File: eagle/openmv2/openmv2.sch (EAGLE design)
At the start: 82 parts, among them J3 CON_HEADER_1X03, J4 CON_HEADER_1X03, Q1 MOSFET, U1 TPS2114APW, U10 IS42S16800E, U2 USD-47571, U3 BEAD, U4 TPS768, U5 BEAD, U6 BEAD, U7 STM32F429, U8 VREG_25, U9 OV2640, X1 USB-MICROB

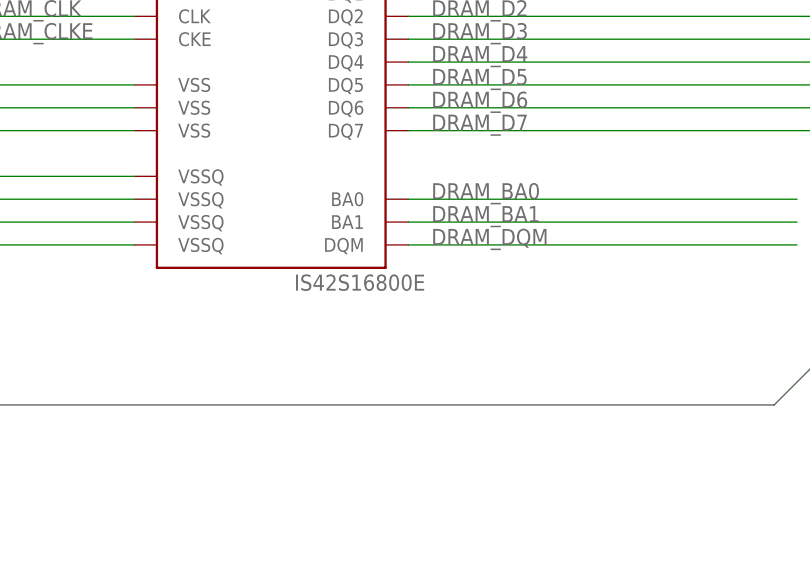
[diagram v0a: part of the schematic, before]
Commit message: Fix SDRAM part-no
* Issue #29
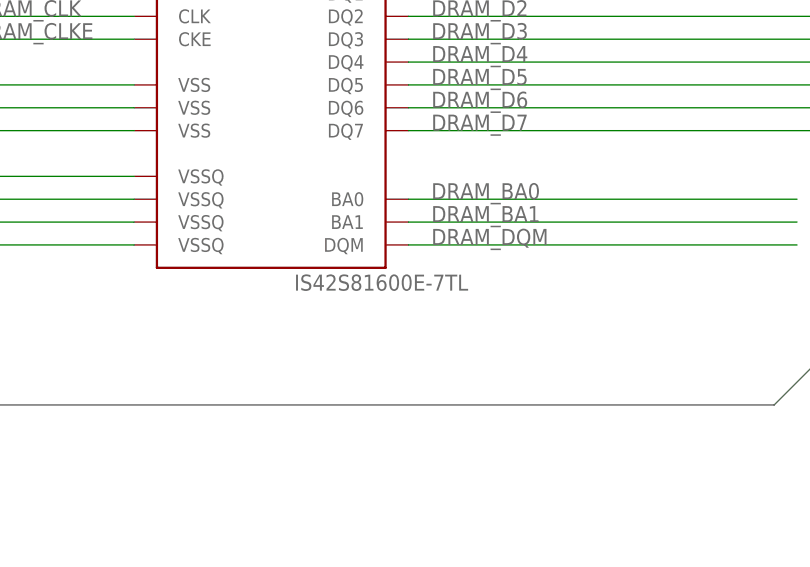
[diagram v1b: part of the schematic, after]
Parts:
- U10: value IS42S16800E -> IS42S81600E-7TL
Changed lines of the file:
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@@
 <part name="C14" library="sfe" deviceset="CAP" device="0402-CAP" value="0.1uF"/>
 <part name="GND3" library="sfe" deviceset="GND" device=""/>
-<part name="U10" library="mux" deviceset="IS42S16800E" device=""/>
+<part name="U10" library="mux" deviceset="IS42S16800E" device="" value="IS42S81600E-7TL"/>
 <part name="U9" library="omnivision" deviceset="OV2640" device=""/>
 <part name="C16" library="sfe" deviceset="CAP" device="0402-CAP" value="0.1uF"/>

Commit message: Rename Eagle files
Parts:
- removed C12, C21: 100uF, sfe:CAP_POL1206
- removed C25, C26, C27, C28, C29, C31, C32, C35, C36, C37, C43: 0.1uF, sfe:CAP0402-CAP
- removed C30: 10uF, sfe:CAP0805
- removed C33, C34: 2.2uF, sfe:CAP0402-CAP
- removed C38: 100uF, sfe:CAP_POL3528
- removed H1, H8: MOUNT-PAD-ROUND2.8, holes:MOUNT-PAD-ROUND2.8
- removed R12: 1K, sfe:RESISTOR0402-RES
- removed R4: 10ohm, iofault:RESISTOR0402-RES
- removed RN2, RN8: (no value), resistor-dil:4R-NCAT16
- removed U$1: LENSMOUNT, omnivision:LENSMOUNT
- removed U$14, U$15, U$16, U$17, U$19, U$20: FIDUCIAL, adafruit:FIDUCIAL
- removed U10: IS42S81600E-7TL, mux:IS42S16800E
- removed U5: BEAD, heka:BEAD
- removed X1: USB-MICROB, sfe:USB-MICROB
- added C48, C49: 2.2uF, sfe:CAP0603-CAP
- added D1: BAT54C, diode:BAT54C
- added JP3, JP4: (no value), pinhead:PINHD-1X8
- added JP5, JP6, JP7, JP8: FIDUCIAL1X2, sfe:FIDUCIAL1X2
- added R2: 10k, sfe:RESISTOR0603-RES
- added U12: STM32F427-LQFP100, mux:STM32F407LQFP100
- added X2: USB-MICROB, sfe:USB-MICROB
- C1: value 0.1uF -> 22uF; device sfe:CAP0402-CAP -> sfe:CAP0805
- C10, C13, C14, C15, C16, C17, C18, C19, C20, C4, C5, C6, C7, C8, C9: device sfe:CAP0402-CAP -> sfe:CAP0603-CAP
- C11: value 100uF -> 22uF; device sfe:CAP_POL3528 -> sfe:CAP0805
- C2: value 0.1uF -> 4.7uF; device sfe:CAP0402-CAP -> sfe:CAP0603-CAP
- C23, C24: value 10uF -> 4.7uF; device sfe:CAP0402-CAP -> sfe:CAP0603-CAP
- C3: device sfe:CAP_POL1206 -> sfe:CAP1206
- C40, C41: value 18pF -> 12pF; device sfe:CAP0402-CAP -> sfe:CAP0603-CAP
- JP1, JP2: value (none) -> FIDUCIAL1X2; device pinhead:PINHD-1X10 -> sfe:FIDUCIAL1X2
- LOGO1: value OSHW_LOGO_FILLX0200-NT -> OSHW_LOGO_FILLX0150-NT; device iofault:OSHW_LOGO_FILLX0200-NT -> iofault:OSHW_LOGO_FILLX0150-NT
- R1: value 10K -> 10ohm; device sfe:RESISTOR0402-RES -> sfe:RESISTOR0603-RES
- R5: device sfe:RESISTOR0402-RES -> sfe:RESISTOR0603-RES
- RN4: value (none) -> 220R; device resistor-dil:4R-NCAT16 -> resistor-dil:4R-NEXBV8V
- RN5, RN6: value (none) -> 10K; device resistor-dil:4R-NCAT16 -> resistor-dil:4R-NEXBV8V
- RN7: value (none) -> 10K
- U1: value TPS2114APW -> LENSMOUNT20MM; device mux:TPS2115APW -> omnivision:LENSMOUNT20MM
- U3, U6: value BEAD -> (none); device heka:BEAD -> sfe:INDUCTOR0603
- U4: value TPS768 -> BD33IA; device mux:TPS768 -> mux:BD33IA
- U7: value STM32F429 -> (none); device stm32:STM32F429 -> sfe:INDUCTOR0603
- U8: value VREG_25 -> VREG_28
- Y1: device mux:CRYSTAL -> mux:CRYSTAL2.5X2.0
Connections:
- removed net ADC12_IN14: JP1.8, U7G$2.PC4/ETH_RMII_RX_D0/ETH_MII_RX_D0/ADC12_IN14
- removed net ADC12_IN15: JP1.7, U7G$2.PC5/ETH_RMII_RX_D1/ETH_MII_RX_D1/ADC12_IN15
- removed net ADC12_IN5: U7G$2.PA5/SPI1_SCK/OTG_HS_ULPI_CK/TIM2_CH1/TIM2_ETR/TIM8_CHIN/ADC12_IN5
- removed net DCMI_SCL: RN7B.1, U7G$2.PB10/SPI2_SCK/I2S2_CK/I2C2_SCL/USART3_TX/OTG_HS_ULPI_D3/TIM2_CH3, U9.SCL
- removed net DCMI_SDA: RN7A.1, U7G$2.PB11/I2C2_SDA/USART3_RX/OTG_HS_ULPI_D4/ETH_RMII_TX_EN/TIM2_CH4, U9.SDA
- removed net DRAM_A0: U10.A0, U7G$3.PF0/I2C2_SDA/FMC_A0
- removed net DRAM_A1: U10.A1, U7G$3.PF1/I2C2_SCL/FMC_A1
- removed net DRAM_A10: U10.A10, U7G$3.PG0/FMC_A10
- removed net DRAM_A11: U10.A11, U7G$3.PG1/FMC_A11
- removed net DRAM_A2: U10.A2, U7G$3.PF2/I2C2_SMBA/FSMC_A2
- removed net DRAM_A3: U10.A3, U7G$3.PF3/FMC_A3
- removed net DRAM_A4: U10.A4, U7G$3.PF4/FMC_A4
- removed net DRAM_A5: U10.A5, U7G$3.PF5/FMC_A5
- removed net DRAM_A6: U10.A6, U7G$3.PF12/FMC_A6
- removed net DRAM_A7: U10.A7, U7G$3.PF13/FMC_A7
- removed net DRAM_A8: U10.A8, U7G$3.PF14/FMC_A8
- removed net DRAM_A9: U10.A9, U7G$3.PF15/FMC_A9
- removed net DRAM_BA0: U10.BA0, U7G$3.PG4/FMC_A14/FMC_BA0
- removed net DRAM_BA1: U10.BA1, U7G$3.PG5/FMC_A15/FMC_BA1
- removed net DRAM_CAS: U10.!CAS, U7G$3.PG15/USART6_CTS/DCMI_D13/FMC_SDNCAS
- removed net DRAM_CLK: U10.CLK, U7G$3.PG8/SPI6_NSS/USART6_RTS/ETH_PPS_OUT/FMC_SDCLK
- removed net DRAM_CLKE: U10.CKE, U7G$3.PC3/SPI2_MOSI/I2S2_SD/OTG_HS_ULPI_NXT/ETH_MII_TX_CLK/FMC_SDCKE0
- removed net DRAM_CS: R1.2, U10.!CS, U7G$3.PC2/SPI2_MISO/I2S2EXT_SD/OTG_HS_ULPI_DIR/ETH_MII_TXD2/FMC_SDNE0
- removed net DRAM_D0: U10.DQ0, U7G$3.PD14/FMC_D0/TIM4_CH3
- removed net DRAM_D1: U10.DQ1, U7G$3.PD15/FMC_D1/TIM4_CH4
- removed net DRAM_D2: U10.DQ2, U7G$3.PD0/FMC_D2/CAN1_RX
- removed net DRAM_D3: U10.DQ3, U7G$3.PD1/FMC_D3/CAN1_TX
- removed net DRAM_D4: U10.DQ4, U7G$3.PE7/FMC_D4/TIM1_ETR/UART7_RX
- removed net DRAM_D5: U10.DQ5, U7G$3.PE8/FSMC_D5/TIM1_CH1N/UART7_TX
- removed net DRAM_D6: U10.DQ6, U7G$3.PE9/FMC_D6/TIM1_CH1
- removed net DRAM_D7: U10.DQ7, U7G$3.PE10/FMC_D7/TIM1_CH2N
- removed net DRAM_DQM: U10.DQM, U7G$3.PE0/TIM4_ETR/UART8_RX/FMC_NBL0/DCMI_D2
- removed net DRAM_RAS: U10.!RAS, U7G$3.PF11/DCMI_12/SPI5_MOSI/FMC_SDNRAS
- removed net DRAM_WE: U10.!WE, U7G$3.PC0/OTG_HS_ULPI_STP/ADC123_IN10/FMC_SDNWE
- removed net FS_DN: U7G$2.PA11/TIM1_CH4/USART1_CTS/CAN1_RX/LCD_R4/OTG_FS_DM, X1.D-
- removed net N$15: U7G$2.PG13/SPI6_SCK/USART6_CTS/ETH_MII_TXD0/ETH_RMII_TXD0/FMC_A24
- removed net N$17: U7G$2.PG7/FSMC_INT3/DCMI_D13
- removed net N$18: U7G$2.PF6/TIM10_CH1/SPI5_NSS/SAI1_SD_B/UART7_RX/FMC_NIORD
- removed net N$19: U7G$2.PG6/FSMC_INT2/DCMI_D12
- removed net N$20: JP1.1, RN8A.1
- removed net N$21: JP1.2, RN8B.1
- removed net N$22: U5.1, X1.VBUS
- removed net N$23: JP1.3, RN8C.1
- removed net N$24: JP1.4, RN8D.1
- removed net N$25: U7G$2.PD6/SPI3_MOSI/I2S3_SD/USART2_RX/FMC_NWAIT/DCMI_D10
- removed net N$26: R12.2, U1.LIMIT
- removed net N$27: U7G$2.PF7/TIM11_CH1/SPI5_SCK/SAI1_MCLK_B/UART7_TX/FMC_NREG
- removed net N$28: U7G$2.PF8/TIM13_CH1/SPI5_MISO/SAI1_SCK_B/FMC_NIOWR
- removed net SPI4_MISO: RN8C.2, U7G$2.PE5/TRACED2/FSMC_A21/TIM9_CH1/DCMI_D6/SPI4_MISO
- removed net SPI4_MOSI: RN8D.2, U7G$2.PE6/TRACED3/FSMC_A22/TIM9_CH2/DCMI_D7/SPI4_MOSI
- removed net SPI4_NSS: RN8B.2, U7G$2.PE3/TRACED0/FSMC_A19
- removed net SPI4_SCK: RN8A.2, U7G$2.PE2/TRACECLK/FSMC_A23/ETH_MII_TXD3/SPI4_SCK
- removed net TIM12_CH1: U7G$2.PB14/SPI2_MISO/TIM1_CH2N/TIM12_CH1/OTG_HS_DM/USART3_RTS/TIM8_CH2N
- removed net TIM12_CH2: U7G$2.PB15/SPI2_MOSI/I2S2_SD/TIM1_CH3N/TIM8_CH3N/TIM12_CH2/OTG_HS_DP
- removed net USART2_RX: JP1.6, U7G$2.PA3/USART2_RX/TIM5_CH4/TIM9_CH2/TIM2_CH4/OTG_HS_ULPI_D0
- removed net USART2_TX: JP1.5, U7G$2.PA2/USART2_TX/TIM5_CH3/TIM9_CH1/TIM2_CH3/ETH_MDIO
- removed net USART3_RX: JP2.7, U7G$2.PD9/FMC_D14/USART3_RX
- removed net USART3_TX: JP2.8, U7G$2.PD8/FMC_D13/USART3_TX
- removed net VBAT: J3.2, J4.2, JP2.9, U1.IN2
- new net DAC: JP4.7, U12.PA5/SPI1_SCK/OTG_HS_ULPI_CK/TIM2_CH1_ETR/TIM8_CHIN/ADC12_IN5
- new net EXPST: U12.PD8/FSMC_D13/USART3_TX, U9.EXPST_B
- new net FREX: U12.PD9/FSMC_D14/USART3_RX, U9.FREX
- new net FS_DM: U12.PA11/USART1_CTS/CAN1_RX/TIM1_CH4/OTG_FS_DM, X2.D-
- new net I2C1_SCL: RN7B.1, U12.PB8/TIM4_CH3/SDIO_D4/TIM10_CH1/DCMI_D6/OTG_FS_SCL/ETH_MII_TXD3, U9.SCL
- new net I2C1_SDA: RN7A.1, U12.PB9/SPI2_NSS/I2S2_WS/TIM4_CH4/TIM11_CH1/SDIO_D5/DCMI_D7/I2C1_SDA, U9.SDA
- new net I2C2_SCL: JP4.5, U12.PB10/SPI2_SCK/I2S2_CK/I2C2_SCL/USART3_TX/OTG_HS_ULPI_D3/TIM2_CH3
- new net I2C2_SDA: JP4.6, U12.PB11/I2C2_SDA/USART3_RX/OTG_HS_ULPI_D4/ETH_RMII_TX_EN/TIM2_CH4
- new net RAW: D1.A1, J3.2, J4.2, JP3.7
- new net SPI2_MISO: JP4.2, U12.PB14/SPI2_MISO/TIM1_CH2N/TIM12_CH1/OTG_HS_DMUSART3_/53/RTS/TIM8_CH2N
- new net SPI2_MOSI: JP4.1, U12.PB15/SPI2_MOSI/I2S2_SD/TIM1_CH3N/TIM8_CH3N/TIM12_CH2/OTG_HS_DP
- new net SPI2_NSS: JP4.4, U12.PB12/SPI2_NSS/I2S2_WS/I2C2_SMBA/USART3_CK/TIM1_BKIN/CAN2_RX
- new net SPI2_SCLK: JP4.3, U12.PB13/SPI2_SCK/I2S2_CK/USART3_CTS/TIM1_CH1N/CAN2_TX/OTG_HS_ULPI_D6
- new net STROBE: U12.PD3/FSMC_CLK/USART2_CTS, U9.STROBE
- net BOOT0: now also JP3.3, RN5A.2, U12.BOOT0; no longer JP2.3, RN2C.2, U7G$1.BOOT0
- net DCMI_CLK: now also U12.PA8/MCO1/USART1_CK/TIM1_CH1/I2C3_SCL/OTG_FS_SOF; no longer U7G$2.PA8/MCO1/USART1_CK/TIM1_CH1/I2C3_SCL/OTG_FS_SOF
- net DCMI_D0: now also U12.PC6/I2S2_MCK/TIM8_CH1/SDIO_D6/USART6_TX/DCMI_D0/TIM3_CH1; no longer U7G$4.PC6/I2S2_MCK/TIM8_CH1/SDIO_D6/USART6_TX/DCMI_D0
- net DCMI_D1: now also U12.PC7/I2S3_MCK/TIM8_CH2/SDIO_D7/USART6_RX/DCMI_D1/TIM3_CH2; no longer U7G$4.PC7/I2S3_MCK/TIM8_CH2/SDIO_D7/USART6_RX/DCMI_D1
- net DCMI_D2: now also U12.PE0/TIM4_ETR/FSMC_NBL0/DCMI_D2; no longer U7G$4.PG10/LCD_G3/FMC_NCE4_1/FMC_NE3/DCMI_D2/LCD_B2
- net DCMI_D3: now also U12.PE1/FSMC_NBL1/DCMI_D3; no longer U7G$4.PG11/ETH_MII_TX_EN/ETH_RMII_TX_ENFMC_NCE4_2/DCMI_D3
- net DCMI_D4: now also U12.PE4/TRACED1/FSMC_A20/DCMI_D4; no longer U7G$4.PE4/TRACED1/FSMC_A20/DCMI_D4/SPI4_NSS
- net DCMI_D5: now also U12.PB6/I2C1_SCL/TIM4_CH1/CAN2_TX/OTG_FS_INTN/DCMI_D5/USART1_TX; no longer U7G$4.PD3/SPI2_SCK/I2S2_CK/USART2_CTS/FMC_CLK/DCMI_D5
- net DCMI_D6: now also U12.PE5/TRACED2/FSMC_A21/TIM9_CH1/DCMI_D6; no longer U7G$4.PB8/TIM4_CH3/TIM10_CH1/I2C1_SCL/CAN1_RX/SDIO_D4/DCMI_D6
- net DCMI_D7: now also U12.PE6/TRACED3/FSMC_A22/TIM9_CH2/DCMI_D7; no longer U7G$4.PB9/TIM11_CH1/I2C1_SDA/SPI2_NSS/I2S2_WS/SDIO_D5/DCMI_D7
- net DCMI_HSYNC: now also U12.PA4/SPI1_NSS/SPI3_NSS/USART2_CK/DCMI_HSYNC/OTG_HS_SOF/I2S3_WS; no longer U7G$4.PA4/SPI1_NSS/SPI3_NSS/USART2_CK/DCMI_HSYNC
- net DCMI_PCLK: now also U12.PA6/SPI1_MISO/TIM8_BKIN/TIM13_CH1/DCMI_PIXCLK/TIM3_CH1/TIM1_BKIN; no longer U7G$4.PA6/SPI1_MISO/TIM8_BKIN/TIM13_CH1/DCMI_PIXCLK
- net DCMI_PWDN: now also U12.PB5/I2C1_SMBA/TIM3_CH2/SPI1_MOSI/SPI3_MOSI/DCMI_D10/I2S3_SD; no longer U7G$2.PA10/TIM1_CH3/USART1_RX/OTG_FS_ID/DCMI_D1
- net DCMI_RST: now also U12.PA10/USART1_RX/TIM1_CH3/OTG_FS_ID/DCMI_D1; no longer U7G$2.PA15/JTDI/SPI3_NSS/I2S3_WS/TIM2_CH1_ETR/SPI1_NSS
- net DCMI_VSYNC: now also U12.PB7/I2C1_SDA/FSMC_NL/DCMI_VSYNC/USART1_RX/TIM4_CH2; no longer U7G$4.PB7/TIM4_CH2//I2C1_SDA/USART1_RX//FMC_NL/DCMI_VSYNC
- net FS_DP: now also U12.PA12/USART1_RTS/CAN1_TX/TIM1_ETR/OTG_FS_DP, X2.D+; no longer U7G$2.PA12/TIM1_ETR/USART1_RTS/CAN1_TX/LCD_R5/OTG_FS_DP, X1.D+
- net GND: now also C11.1, C3.2, C48.2, C49.2, JP3.8, R2.1, RN5A.1, U12.PB2/BOOT1, U12.VSS@1, U12.VSS@2, U12.VSS@3, U12.VSS@4, U12.VSSA, U4.GND@1, U4.GND@2, X2.GND; no longer C11.-, C12.-, C21.-, C25.2, C26.2, C27.2, C28.1, C29.2, C3.-, C30.2, C31.2, C32.2, C33.2, C34.2, C35.2, C36.2, C37.2, C38.-, C43.2, H1.MOUNT, H2.MOUNT, H6.MOUNT, H8.MOUNT, JP1.10, JP2.10, R12.1, RN2A.1, RN2C.1, U$1.P$1, U$1.P$2, U1.D1, U1.GND, U10.VSS@1, U10.VSS@2, U10.VSS@3, U10.VSSQ@1, U10.VSSQ@2, U10.VSSQ@3, U10.VSSQ@4, U4.EN, U4.GND, U7G$1.BOOT1, U7G$1.VSS@1, U7G$1.VSS@2, U7G$1.VSS@3, U7G$1.VSS@4, U7G$1.VSS@5, U7G$1.VSS@6, U7G$1.VSS@7, U7G$1.VSS@8, U7G$1.VSS@9, U7G$1.VSSA, U9.EXPST_B, U9.FREX, X1.GND
- net LED_B: now also U12.PC1/ETH_MDC/ADC123_IN11; no longer U7G$2.PB5/TIM3_CH2/SPI1_MOSI/SPI3_MOSI/I2S3_SD/DCMI_D10/FMC_SDCKE1
- net LED_G: now also U12.PC2/SPI2_MISO/OTG_HS_ULPI_DIR/TH_MII_TXD2/I2S2EXT_SD/ADC123_IN12; no longer U7G$2.PB6/TIM4_CH1/I2C1_SCL/USART1_TX/CAN2_TX/FMC_SDNE1/DCMI_D5
- net LED_IR: now also U12.PE2/TRACECLK/FSMC_A23/ETH_MII_TXD3; no longer U7G$2.PB3/JTDO/TRACESWO/SPI3_SCK/I2S3_CK/TIM2_CH2/SPI1_SCK
- net LED_R: now also U12.PC0/OTG_HS_ULPI_STP/ADC123_IN10; no longer U7G$2.PB4/NJTRST/TIM3_CH1/SPI1_MISO/SPI3_MISO/I2S3EXT_SD
- net N$10: now also R1.2; no longer R4.1
- net N$12: now also C4.1, C5.1, U12.VDDA, U12.VREF, U3.1; no longer U7G$2.PG12/SPI6_MISO/USART6_RTS/LCD_B4/FMC_NE4/LCD_B1
- net N$14: now also R1.1; no longer R4.2
- net N$2: now also U12.PH1/OSC_OUT; no longer U7G$1.PH0/OSC_IN
- net N$4: now also U12.PH0/OSC_IN; no longer U7G$1.PH1/OSC_OUT
- net N$5: now also R2.2
- net N$7: now also U7.1, X2.VBUS; no longer C4.1, C5.1, U3.1, U7G$1.VDDA, U7G$1.VREF+
- net NRST: now also JP3.4, RN5B.2, U12.NRST; no longer JP2.4, RN2D.2, U7G$1.NRST
- net SDIO_CLK: now also U12.PC12/UART5_TX/SDIO_CK/DCMI_D9/SPI3_MOSI/I2S3_SD/USART3_CK; no longer U7G$2.PC12/UART5_TX/SDIO_CK/DCMI_D9/SPI3_MOSI/I2S3_SD/USART3_CK
- net SDIO_CMD: now also U12.PD2/TIM3_ETR/UART5_RXSDIO_CMD/DCMI_D11; no longer U7G$2.PD2/TIM3_ETR/UART5_RX/SDIO_CMD/DCMI_D11
- net SDIO_D0: now also RN5C.2, U12.PC8/TIM8_CH3/SDIO_D0/TIM3_CH3/USART6_CK/DCMI_D2; no longer RN5B.2, U7G$2.PC8/TIM8_CH3/SDIO_D0/TIM3_CH3/USART6_CK/DCMI_D2
- net SDIO_D1: now also U12.PC9/I2S_CKIN/MCO2/TIM8_CH4/SDIO_D1/I2C3_SDA/DCMI_D3/TIM3_CH4; no longer U7G$2.PC9/I2S_CKIN/MCO2/TIM8_CH4/SDIO_D1/I2C3_SDA/DCMI_D3/TIM3_CH4
- net SDIO_D2: now also U12.PC10/SPI3_SCK/I2S3_CK/UART4_TX/SDIO_D2/DCMI_D8/USART3_TX; no longer U7G$2.PC10/SPI3_SCK/I2S3_CK/UART4_TX/SDIO_D2/DCMI_D8/USART3_TX
- net SDIO_D3: now also U12.PC11/UART4_RX/SPI3_MISO/SDIO_D3/DCMI_D4/USART3_RX/I2S3EXT_SD; no longer U7G$2.PC11/UART4_RX/SPI3_MISO/SDIO_D3/DCMI_D4
- net SD_CD: now also U12.PA15/JTDI/SPI3_NSS/I2S3_WS/TIM2_CH1_ETR/SPI1_NSS; no longer U7G$2.PG9/USART6_RX/FMC_NE2/FMC_NCE3/DCMI_VSYNC
- net SWCLK: now also JP3.1, U12.PA14/JTCK-SWCLK; no longer JP2.1, RN2A.2, U7G$1.PA14/JTCK-SWCLK
- net SWDIO: now also JP3.2, U12.PA13/JTMS-SWDIO; no longer JP2.2, RN2B.2, U7G$1.PA13/JTMS-SWDIO
- net TIM4_CH1: now also JP3.6, U12.PD12/FSMC_A17/TIM4_CH1/USART3_RTS; no longer JP2.6, U7G$2.PD12/FMC_A17/TIM4_CH1/USART3_RTS
- net TIM4_CH2: now also JP3.5, U12.PD13/FSMC_A18/TIM4_CH2; no longer JP2.5, U7G$2.PD13/FMC_A18/TIM4_CH2
- net VBUS: now also D1.A2, U12.PA9/USART1_TX/TIM1_CH2/I2C3_SMBA/DCMI_D0/OTG_FS_VBUS, U7.2; no longer C43.1, U1.IN1, U5.2, U7G$2.PA9/TIM1_CH2/I2C3_SMBA/USART1_TX/DCMI_D0/OTG_FS_VBUS
- net VCAP1: now also C49.1, U12.VCAP@1; no longer C34.1, U7G$1.VCAP@1
- net VCAP2: now also C48.1, U12.VCAP@2; no longer C33.1, U7G$1.VCAP@2
- net VCC: now also C11.2, C3.1, JP4.8, U12.VBAT, U12.VDD@1, U12.VDD@2, U12.VDD@3, U12.VDD@4, U12.VDD@5, U12.VDD@6, U4.VO, U4.VOS; no longer C12.+, C2.1, C21.+, C25.1, C26.1, C27.1, C28.2, C29.1, C3.+, C30.1, C31.1, C32.1, C35.1, C36.1, C37.1, C38.+, JP1.9, R1.1, RN2B.1, RN2D.1, RN5A.1, U10.VDD@1, U10.VDD@2, U10.VDD@3, U10.VDDQ@1, U10.VDDQ@2, U10.VDDQ@3, U10.VDDQ@4, U4.OUT@1, U4.OUT@2, U7G$1.PDR_ON, U7G$1.VBAT, U7G$1.VDD@1, U7G$1.VDD@10, U7G$1.VDD@11, U7G$1.VDD@12, U7G$1.VDD@2, U7G$1.VDD@3, U7G$1.VDD@4, U7G$1.VDD@5, U7G$1.VDD@6, U7G$1.VDD@7, U7G$1.VDD@8, U7G$1.VDD@9
- net VIN: now also C2.1, D1.CC, U4.EN, U4.VCC; no longer C11.+, U1.OUT, U4.IN@1, U4.IN@2
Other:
- note removed: "USB lines are terminated in driver"
- moved on the sheet: C1, C10, C13, C14, C15, C16, C17, C18, C19, C2, C20, C23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

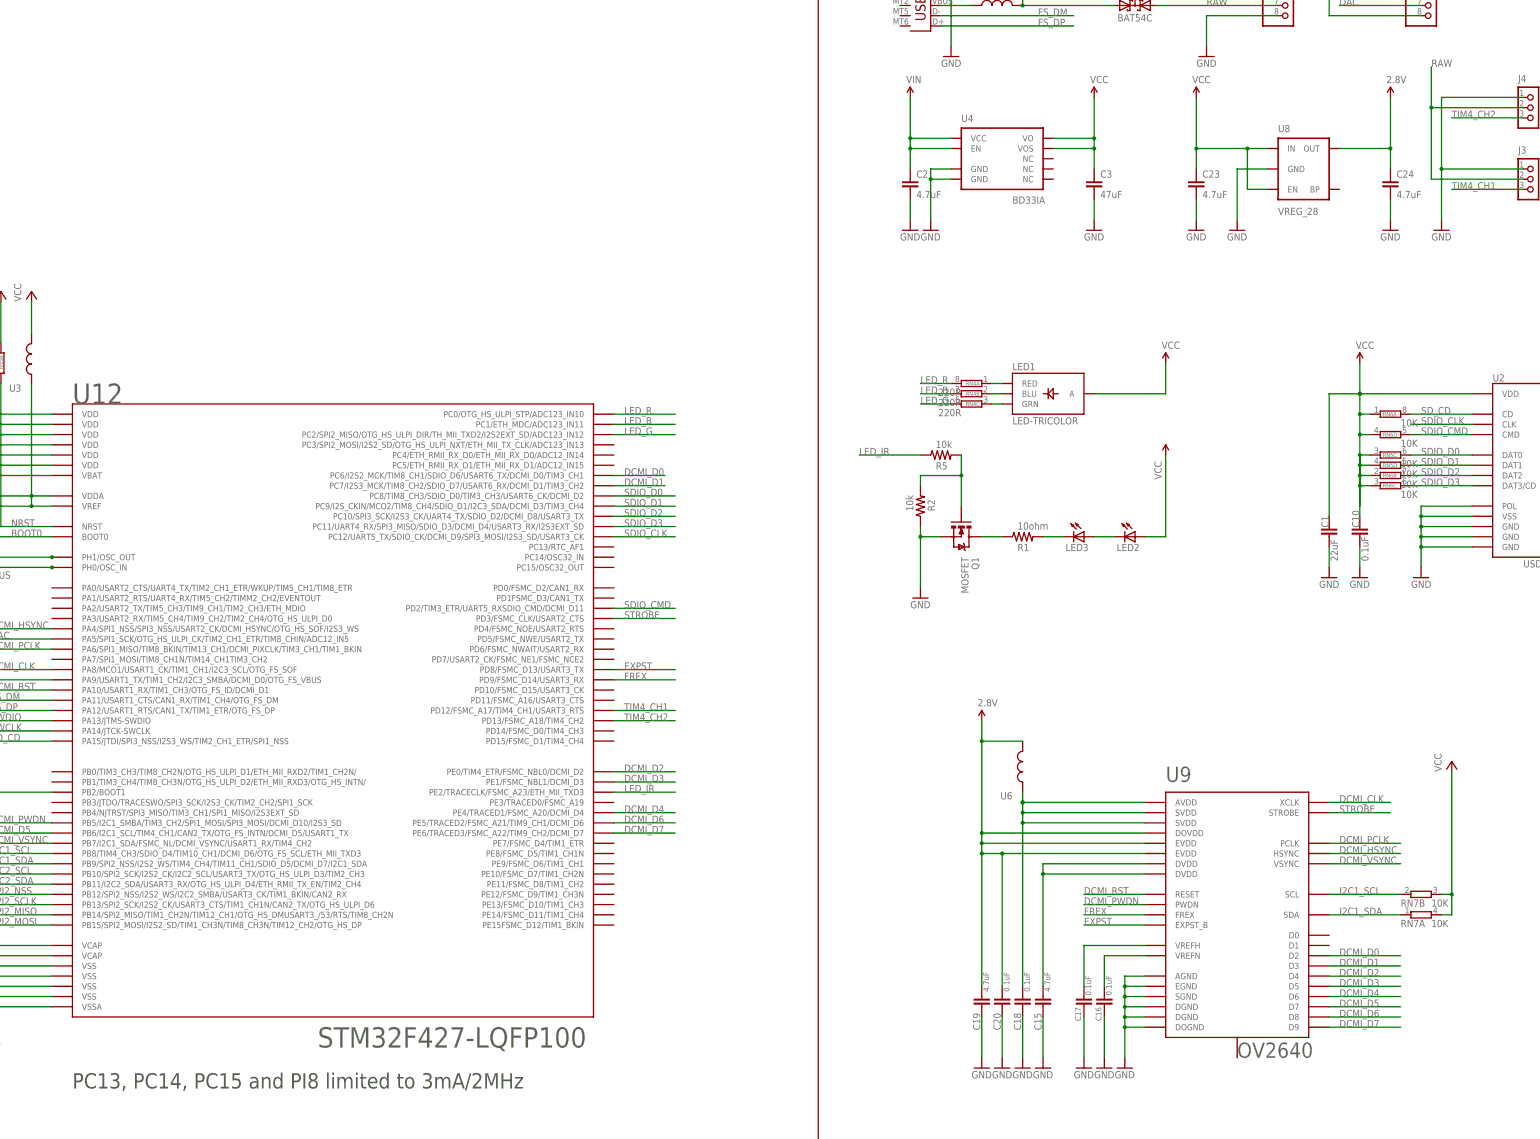
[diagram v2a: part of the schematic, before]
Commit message: Update Eagle files.
* Add OpenMV2-R5
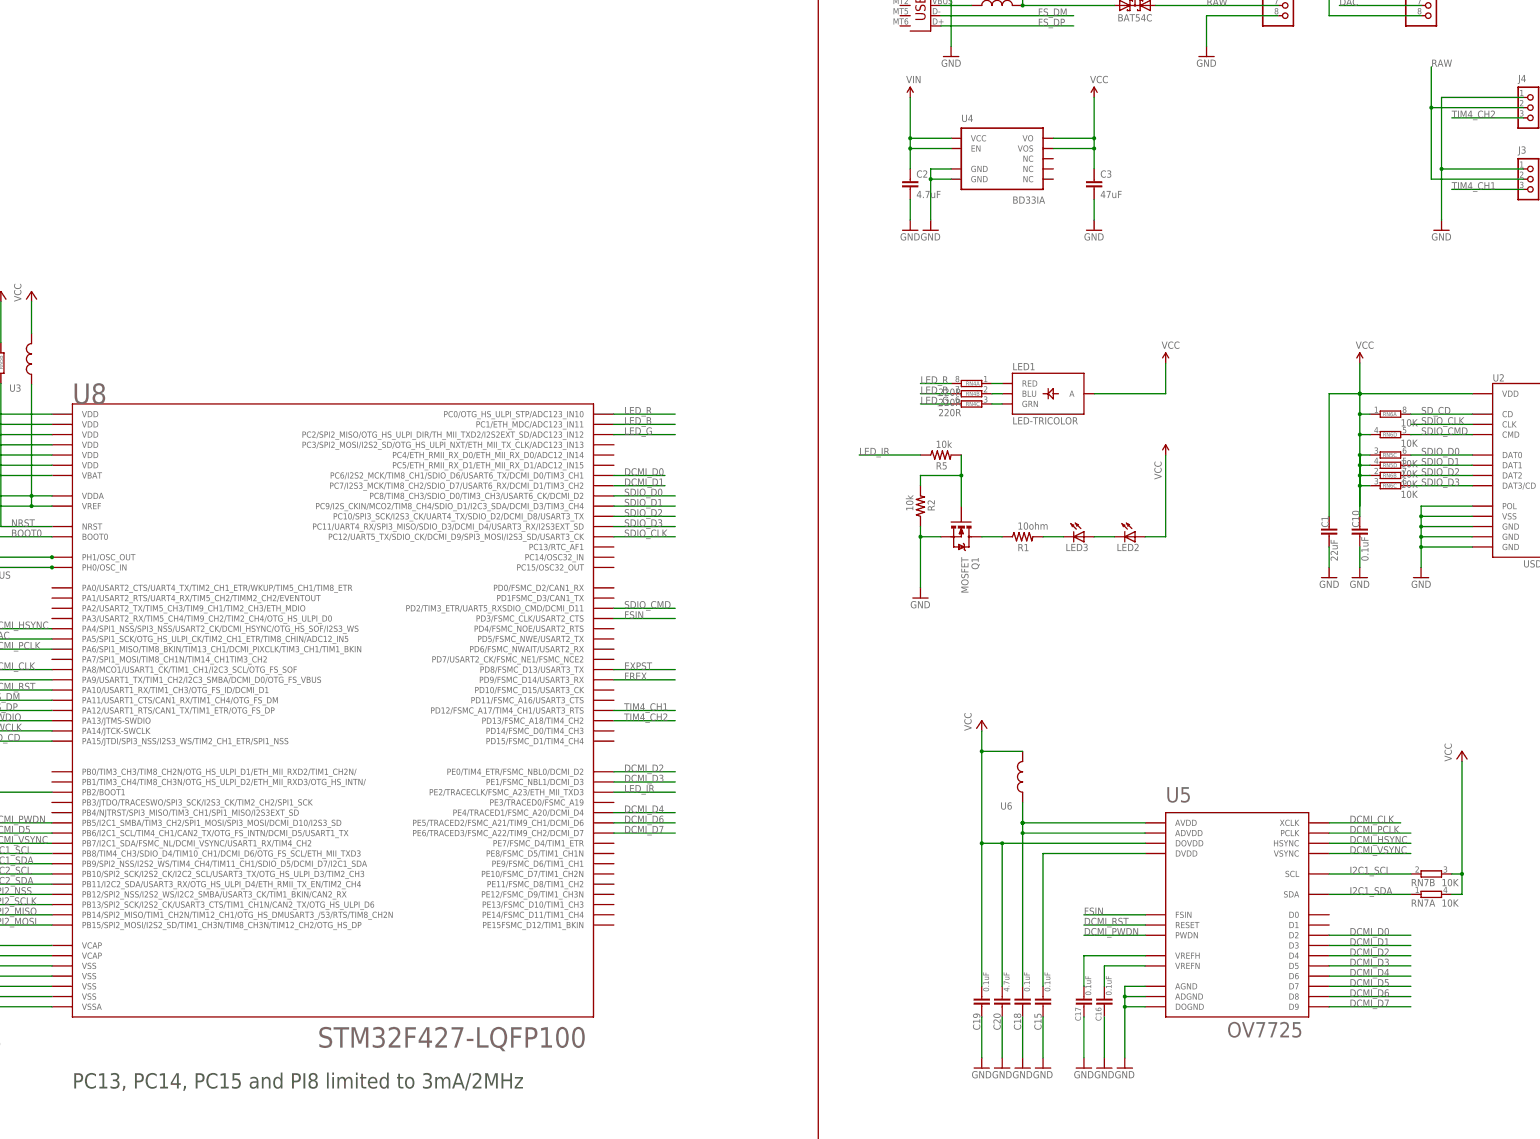
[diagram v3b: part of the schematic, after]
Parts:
- removed C23, C24: 4.7uF, sfe:CAP0603-CAP
- removed U12: STM32F427-LQFP100, mux:STM32F407LQFP100
- removed U9: OV2640, omnivision:OV2640
- added U5: OV7725, omnivision:OV7725
- C15, C19: value 4.7uF -> 0.1uF
- C20: value 0.1uF -> 4.7uF
- U8: value VREG_28 -> STM32F427-LQFP100; device sfe:V_REG_LDOSMD -> mux:STM32F407LQFP100
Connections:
- removed net 2.8V: C19.1, C20.1, C24.1, U6.2, U8.OUT, U9.DOVDD, U9.EVDD@1, U9.EVDD@2
- removed net N$6: C15.1, U9.DVDD@1, U9.DVDD@2
- removed net STROBE: U12.PD3/FSMC_CLK/USART2_CTS, U9.STROBE
- new net FSIN: U5.FSIN, U8.PD3/FSMC_CLK/USART2_CTS
- new net N$15: C15.1, U5.DVDD
- net BOOT0: now also U8.BOOT0; no longer U12.BOOT0
- net DAC: now also U8.PA5/SPI1_SCK/OTG_HS_ULPI_CK/TIM2_CH1_ETR/TIM8_CHIN/ADC12_IN5; no longer U12.PA5/SPI1_SCK/OTG_HS_ULPI_CK/TIM2_CH1_ETR/TIM8_CHIN/ADC12_IN5
- net DCMI_CLK: now also U5.XCLK, U8.PA8/MCO1/USART1_CK/TIM1_CH1/I2C3_SCL/OTG_FS_SOF; no longer U12.PA8/MCO1/USART1_CK/TIM1_CH1/I2C3_SCL/OTG_FS_SOF, U9.XCLK
- net DCMI_D0: now also U5.D2, U8.PC6/I2S2_MCK/TIM8_CH1/SDIO_D6/USART6_TX/DCMI_D0/TIM3_CH1; no longer U12.PC6/I2S2_MCK/TIM8_CH1/SDIO_D6/USART6_TX/DCMI_D0/TIM3_CH1, U9.D2
- net DCMI_D1: now also U5.D3, U8.PC7/I2S3_MCK/TIM8_CH2/SDIO_D7/USART6_RX/DCMI_D1/TIM3_CH2; no longer U12.PC7/I2S3_MCK/TIM8_CH2/SDIO_D7/USART6_RX/DCMI_D1/TIM3_CH2, U9.D3
- net DCMI_D2: now also U5.D4, U8.PE0/TIM4_ETR/FSMC_NBL0/DCMI_D2; no longer U12.PE0/TIM4_ETR/FSMC_NBL0/DCMI_D2, U9.D4
- net DCMI_D3: now also U5.D5, U8.PE1/FSMC_NBL1/DCMI_D3; no longer U12.PE1/FSMC_NBL1/DCMI_D3, U9.D5
- net DCMI_D4: now also U5.D6, U8.PE4/TRACED1/FSMC_A20/DCMI_D4; no longer U12.PE4/TRACED1/FSMC_A20/DCMI_D4, U9.D6
- net DCMI_D5: now also U5.D7, U8.PB6/I2C1_SCL/TIM4_CH1/CAN2_TX/OTG_FS_INTN/DCMI_D5/USART1_TX; no longer U12.PB6/I2C1_SCL/TIM4_CH1/CAN2_TX/OTG_FS_INTN/DCMI_D5/USART1_TX, U9.D7
- net DCMI_D6: now also U5.D8, U8.PE5/TRACED2/FSMC_A21/TIM9_CH1/DCMI_D6; no longer U12.PE5/TRACED2/FSMC_A21/TIM9_CH1/DCMI_D6, U9.D8
- net DCMI_D7: now also U5.D9, U8.PE6/TRACED3/FSMC_A22/TIM9_CH2/DCMI_D7; no longer U12.PE6/TRACED3/FSMC_A22/TIM9_CH2/DCMI_D7, U9.D9
- net DCMI_HSYNC: now also U5.HSYNC, U8.PA4/SPI1_NSS/SPI3_NSS/USART2_CK/DCMI_HSYNC/OTG_HS_SOF/I2S3_WS; no longer U12.PA4/SPI1_NSS/SPI3_NSS/USART2_CK/DCMI_HSYNC/OTG_HS_SOF/I2S3_WS, U9.HSYNC
- net DCMI_PCLK: now also U5.PCLK, U8.PA6/SPI1_MISO/TIM8_BKIN/TIM13_CH1/DCMI_PIXCLK/TIM3_CH1/TIM1_BKIN; no longer U12.PA6/SPI1_MISO/TIM8_BKIN/TIM13_CH1/DCMI_PIXCLK/TIM3_CH1/TIM1_BKIN, U9.PCLK
- net DCMI_PWDN: now also U5.PWDN, U8.PB5/I2C1_SMBA/TIM3_CH2/SPI1_MOSI/SPI3_MOSI/DCMI_D10/I2S3_SD; no longer U12.PB5/I2C1_SMBA/TIM3_CH2/SPI1_MOSI/SPI3_MOSI/DCMI_D10/I2S3_SD, U9.PWDN
- net DCMI_RST: now also U5.RESET, U8.PA10/USART1_RX/TIM1_CH3/OTG_FS_ID/DCMI_D1; no longer U12.PA10/USART1_RX/TIM1_CH3/OTG_FS_ID/DCMI_D1, U9.RESET
- net DCMI_VSYNC: now also U5.VSYNC, U8.PB7/I2C1_SDA/FSMC_NL/DCMI_VSYNC/USART1_RX/TIM4_CH2; no longer U12.PB7/I2C1_SDA/FSMC_NL/DCMI_VSYNC/USART1_RX/TIM4_CH2, U9.VSYNC
- net EXPST: now also U8.PD8/FSMC_D13/USART3_TX; no longer U12.PD8/FSMC_D13/USART3_TX, U9.EXPST_B
- net FREX: now also U8.PD9/FSMC_D14/USART3_RX; no longer U12.PD9/FSMC_D14/USART3_RX, U9.FREX
- net FS_DM: now also U8.PA11/USART1_CTS/CAN1_RX/TIM1_CH4/OTG_FS_DM; no longer U12.PA11/USART1_CTS/CAN1_RX/TIM1_CH4/OTG_FS_DM
- net FS_DP: now also U8.PA12/USART1_RTS/CAN1_TX/TIM1_ETR/OTG_FS_DP; no longer U12.PA12/USART1_RTS/CAN1_TX/TIM1_ETR/OTG_FS_DP
- net GND: now also U5.ADGND, U5.AGND, U5.DOGND, U8.PB2/BOOT1, U8.VSS@1, U8.VSS@2, U8.VSS@3, U8.VSS@4, U8.VSSA; no longer C23.2, C24.2, U12.PB2/BOOT1, U12.VSS@1, U12.VSS@2, U12.VSS@3, U12.VSS@4, U12.VSSA, U8.GND, U9.AGND, U9.DGND@1, U9.DGND@2, U9.DOGND, U9.EGND, U9.SGND
- net I2C1_SCL: now also U5.SCL, U8.PB8/TIM4_CH3/SDIO_D4/TIM10_CH1/DCMI_D6/OTG_FS_SCL/ETH_MII_TXD3; no longer U12.PB8/TIM4_CH3/SDIO_D4/TIM10_CH1/DCMI_D6/OTG_FS_SCL/ETH_MII_TXD3, U9.SCL
- net I2C1_SDA: now also U5.SDA, U8.PB9/SPI2_NSS/I2S2_WS/TIM4_CH4/TIM11_CH1/SDIO_D5/DCMI_D7/I2C1_SDA; no longer U12.PB9/SPI2_NSS/I2S2_WS/TIM4_CH4/TIM11_CH1/SDIO_D5/DCMI_D7/I2C1_SDA, U9.SDA
- net I2C2_SCL: now also U8.PB10/SPI2_SCK/I2S2_CK/I2C2_SCL/USART3_TX/OTG_HS_ULPI_D3/TIM2_CH3; no longer U12.PB10/SPI2_SCK/I2S2_CK/I2C2_SCL/USART3_TX/OTG_HS_ULPI_D3/TIM2_CH3
- net I2C2_SDA: now also U8.PB11/I2C2_SDA/USART3_RX/OTG_HS_ULPI_D4/ETH_RMII_TX_EN/TIM2_CH4; no longer U12.PB11/I2C2_SDA/USART3_RX/OTG_HS_ULPI_D4/ETH_RMII_TX_EN/TIM2_CH4
- net LED_B: now also U8.PC1/ETH_MDC/ADC123_IN11; no longer U12.PC1/ETH_MDC/ADC123_IN11
- net LED_G: now also U8.PC2/SPI2_MISO/OTG_HS_ULPI_DIR/TH_MII_TXD2/I2S2EXT_SD/ADC123_IN12; no longer U12.PC2/SPI2_MISO/OTG_HS_ULPI_DIR/TH_MII_TXD2/I2S2EXT_SD/ADC123_IN12
- net LED_IR: now also U8.PE2/TRACECLK/FSMC_A23/ETH_MII_TXD3; no longer U12.PE2/TRACECLK/FSMC_A23/ETH_MII_TXD3
- net LED_R: now also U8.PC0/OTG_HS_ULPI_STP/ADC123_IN10; no longer U12.PC0/OTG_HS_ULPI_STP/ADC123_IN10
- net N$1: now also U5.VREFH; no longer U9.VREFH
- net N$12: now also U8.VDDA, U8.VREF; no longer U12.VDDA, U12.VREF
- net N$13: now also U5.ADVDD, U5.AVDD; no longer U9.AVDD, U9.SVDD@1, U9.SVDD@2
- net N$2: now also U8.PH1/OSC_OUT; no longer U12.PH1/OSC_OUT
- net N$3: now also U5.VREFN; no longer U9.VREFN
- net N$4: now also U8.PH0/OSC_IN; no longer U12.PH0/OSC_IN
- net NRST: now also U8.NRST; no longer U12.NRST
- net SDIO_CLK: now also U8.PC12/UART5_TX/SDIO_CK/DCMI_D9/SPI3_MOSI/I2S3_SD/USART3_CK; no longer U12.PC12/UART5_TX/SDIO_CK/DCMI_D9/SPI3_MOSI/I2S3_SD/USART3_CK
- net SDIO_CMD: now also U8.PD2/TIM3_ETR/UART5_RXSDIO_CMD/DCMI_D11; no longer U12.PD2/TIM3_ETR/UART5_RXSDIO_CMD/DCMI_D11
- net SDIO_D0: now also U8.PC8/TIM8_CH3/SDIO_D0/TIM3_CH3/USART6_CK/DCMI_D2; no longer U12.PC8/TIM8_CH3/SDIO_D0/TIM3_CH3/USART6_CK/DCMI_D2
- net SDIO_D1: now also U8.PC9/I2S_CKIN/MCO2/TIM8_CH4/SDIO_D1/I2C3_SDA/DCMI_D3/TIM3_CH4; no longer U12.PC9/I2S_CKIN/MCO2/TIM8_CH4/SDIO_D1/I2C3_SDA/DCMI_D3/TIM3_CH4
- net SDIO_D2: now also U8.PC10/SPI3_SCK/I2S3_CK/UART4_TX/SDIO_D2/DCMI_D8/USART3_TX; no longer U12.PC10/SPI3_SCK/I2S3_CK/UART4_TX/SDIO_D2/DCMI_D8/USART3_TX
- net SDIO_D3: now also U8.PC11/UART4_RX/SPI3_MISO/SDIO_D3/DCMI_D4/USART3_RX/I2S3EXT_SD; no longer U12.PC11/UART4_RX/SPI3_MISO/SDIO_D3/DCMI_D4/USART3_RX/I2S3EXT_SD
- net SD_CD: now also U8.PA15/JTDI/SPI3_NSS/I2S3_WS/TIM2_CH1_ETR/SPI1_NSS; no longer U12.PA15/JTDI/SPI3_NSS/I2S3_WS/TIM2_CH1_ETR/SPI1_NSS
- net SPI2_MISO: now also U8.PB14/SPI2_MISO/TIM1_CH2N/TIM12_CH1/OTG_HS_DMUSART3_/53/RTS/TIM8_CH2N; no longer U12.PB14/SPI2_MISO/TIM1_CH2N/TIM12_CH1/OTG_HS_DMUSART3_/53/RTS/TIM8_CH2N
- net SPI2_MOSI: now also U8.PB15/SPI2_MOSI/I2S2_SD/TIM1_CH3N/TIM8_CH3N/TIM12_CH2/OTG_HS_DP; no longer U12.PB15/SPI2_MOSI/I2S2_SD/TIM1_CH3N/TIM8_CH3N/TIM12_CH2/OTG_HS_DP
- net SPI2_NSS: now also U8.PB12/SPI2_NSS/I2S2_WS/I2C2_SMBA/USART3_CK/TIM1_BKIN/CAN2_RX; no longer U12.PB12/SPI2_NSS/I2S2_WS/I2C2_SMBA/USART3_CK/TIM1_BKIN/CAN2_RX
- net SPI2_SCLK: now also U8.PB13/SPI2_SCK/I2S2_CK/USART3_CTS/TIM1_CH1N/CAN2_TX/OTG_HS_ULPI_D6; no longer U12.PB13/SPI2_SCK/I2S2_CK/USART3_CTS/TIM1_CH1N/CAN2_TX/OTG_HS_ULPI_D6
- net SWCLK: now also U8.PA14/JTCK-SWCLK; no longer U12.PA14/JTCK-SWCLK
- net SWDIO: now also U8.PA13/JTMS-SWDIO; no longer U12.PA13/JTMS-SWDIO
- net TIM4_CH1: now also U8.PD12/FSMC_A17/TIM4_CH1/USART3_RTS; no longer U12.PD12/FSMC_A17/TIM4_CH1/USART3_RTS
- net TIM4_CH2: now also U8.PD13/FSMC_A18/TIM4_CH2; no longer U12.PD13/FSMC_A18/TIM4_CH2
- net VBUS: now also U8.PA9/USART1_TX/TIM1_CH2/I2C3_SMBA/DCMI_D0/OTG_FS_VBUS; no longer U12.PA9/USART1_TX/TIM1_CH2/I2C3_SMBA/DCMI_D0/OTG_FS_VBUS
- net VCAP1: now also U8.VCAP@1; no longer U12.VCAP@1
- net VCAP2: now also U8.VCAP@2; no longer U12.VCAP@2
- net VCC: now also C19.1, C20.1, U5.DOVDD, U6.2, U8.VBAT, U8.VDD@1, U8.VDD@2, U8.VDD@3, U8.VDD@4, U8.VDD@5, U8.VDD@6; no longer C23.1, U12.VBAT, U12.VDD@1, U12.VDD@2, U12.VDD@3, U12.VDD@4, U12.VDD@5, U12.VDD@6, U8.EN, U8.IN
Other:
- moved on the sheet: RN7A, RN7B, U6
